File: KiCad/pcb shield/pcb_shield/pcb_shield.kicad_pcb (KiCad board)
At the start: 2 copper layers, 190 x 60 mm, 3 parts, among them J1 Raspberry Pi Zero, U1 BOB-09056

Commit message: start with pcb
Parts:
- added A3: Motor Controller Left, Module:Pololu_Breakout-16_15.2x20.3mm, F.Cu at (205.7, 87.6)
- added A4: Motor Controller Right, Module:Pololu_Breakout-16_15.2x20.3mm, F.Cu at (205.7, 110.5)
- added C1: C, Capacitor_THT:CP_Radial_D5.0mm_P2.50mm, F.Cu at (194.3, 81.3)
- added C2: C, Capacitor_THT:CP_Radial_D5.0mm_P2.50mm, F.Cu at (194.3, 104.1)
- added J1: , Connector_PinHeader_2.54mm:PinHeader_2x04_P2.54mm_Vertical, F.Cu at (86.4, 120.6)
- added J10: Motor Conn L, Connector_PinHeader_2.54mm:PinHeader_1x04_P2.54mm_Vertical, F.Cu at (236.2, 77.5)
- added J11: Motor Conn R, Connector_PinHeader_2.54mm:PinHeader_1x04_P2.54mm_Vertical, F.Cu at (236.2, 101.6)
- added J12: Endstop X, Connector_PinHeader_2.54mm:PinHeader_1x02_P2.54mm_Vertical, F.Cu at (172.7, 86.4)
- added J13: Endstop Y, Connector_PinHeader_2.54mm:PinHeader_1x02_P2.54mm_Vertical, F.Cu at (172.7, 78.7)
- added J2: , Connector_PinHeader_2.54mm:PinHeader_2x04_P2.54mm_Vertical, F.Cu at (74.9, 120.6)
- added J3: , Connector_PinHeader_2.54mm:PinHeader_2x04_P2.54mm_Vertical, F.Cu at (158.8, 120.6)
- added J4: , Connector_PinHeader_2.54mm:PinHeader_2x04_P2.54mm_Vertical, F.Cu at (147.3, 120.6)
- added J5: , Connector_PinHeader_2.54mm:PinHeader_2x04_P2.54mm_Vertical, F.Cu at (110.5, 120.6)
- added J6: , Connector_PinHeader_2.54mm:PinHeader_2x04_P2.54mm_Vertical, F.Cu at (99.1, 120.6)
- added J7: , Connector_PinHeader_2.54mm:PinHeader_2x04_P2.54mm_Vertical, F.Cu at (134.6, 120.6)
- added J8: , Connector_PinHeader_2.54mm:PinHeader_2x04_P2.54mm_Vertical, F.Cu at (123.2, 120.6)
- added J9: E_Magnet, Connector_PinHeader_2.54mm:PinHeader_1x02_P2.54mm_Vertical, F.Cu at (172.7, 96.5)
- added Q1: TIP120, Package_TO_SOT_THT:TO-220-3_Vertical, F.Cu at (172.7, 109.2)
- added U2: BOB-09056, BOB-09056:MODULE_BOB-09056, F.Cu at (148.6, 96.5)
- added U3: BOB-09056, BOB-09056:MODULE_BOB-09056, F.Cu at (100.3, 96.5)
- added U4: BOB-09056, BOB-09056:MODULE_BOB-09056, F.Cu at (124.5, 96.5)
- moved A1 49.5 mm to (120.7, 67.3)
- moved U1 2.33 mm to (76.2, 96.5)
- renumbered J1 to A1, A1 to A2
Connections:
- A1 pad 20: GND -> Net-(A1-Pad20)
- A1 pad 24: 14 TXD -> /14 TXD
- A1 pad 25: 18 RXD -> /18 RXD
- A1 pad 4: 4 -> Net-(A1-Pad4)
- A1 pad 6: 17 -> Net-(A1-Pad6)
- A1 pad 7: 27 -> Net-(A1-Pad7)
- A1 pad 8: 22 -> Net-(A1-Pad8)
- A2 pad 15: unconnected-(A1-Pad15) -> /14 TXD
- A2 pad 16: unconnected-(A1-Pad16) -> /18 RXD
- A2 pad 17: unconnected-(A1-Pad17) -> Net-(A2-Pad17)
- A2 pad 18: unconnected-(A1-Pad18) -> Net-(A2-Pad18)
- A2 pad 20: unconnected-(A1-Pad20) -> Net-(A3-Pad16)
- A2 pad 21: unconnected-(A1-Pad21) -> Net-(A2-Pad21)
- A2 pad 23: unconnected-(A1-Pad23) -> Net-(A2-Pad23)
- A2 pad 24: unconnected-(A1-Pad24) -> Net-(A2-Pad24)
- A2 pad 25: unconnected-(A1-Pad25) -> Net-(A2-Pad25)
- A2 pad 26: unconnected-(A1-Pad26) -> Net-(A2-Pad26)
- A2 pad 5: unconnected-(A1-Pad5) -> Net-(A4-Pad2)
- A2 pad 7: unconnected-(A1-Pad7) -> Net-(A2-Pad7)
- U1 pad JP1-1: unconnected-(U1-PadJP1-1) -> Net-(U1-PadJP1-1)
- U1 pad JP1-10: unconnected-(U1-PadJP1-10) -> Net-(U1-PadJP1-10)
- U1 pad JP1-11: unconnected-(U1-PadJP1-11) -> Net-(U1-PadJP1-11)
- U1 pad JP1-12: unconnected-(U1-PadJP1-12) -> Net-(U1-PadJP1-12)
- U1 pad JP1-13: unconnected-(U1-PadJP1-13) -> Net-(U1-PadJP1-13)
- U1 pad JP1-14: unconnected-(U1-PadJP1-14) -> Net-(U1-PadJP1-14)
- U1 pad JP1-15: unconnected-(U1-PadJP1-15) -> Net-(U1-PadJP1-15)
- U1 pad JP1-16: unconnected-(U1-PadJP1-16) -> Net-(U1-PadJP1-16)
- U1 pad JP1-2: unconnected-(U1-PadJP1-2) -> Net-(U1-PadJP1-2)
- U1 pad JP1-3: unconnected-(U1-PadJP1-3) -> Net-(U1-PadJP1-3)
- U1 pad JP1-4: unconnected-(U1-PadJP1-4) -> Net-(U1-PadJP1-4)
- U1 pad JP1-5: unconnected-(U1-PadJP1-5) -> Net-(U1-PadJP1-5)
- U1 pad JP1-6: unconnected-(U1-PadJP1-6) -> Net-(U1-PadJP1-6)
- U1 pad JP1-7: unconnected-(U1-PadJP1-7) -> Net-(U1-PadJP1-7)
- U1 pad JP1-8: unconnected-(U1-PadJP1-8) -> Net-(U1-PadJP1-8)
- U1 pad JP1-9: unconnected-(U1-PadJP1-9) -> Net-(U1-PadJP1-9)
- U1 pad JP3-1: unconnected-(U1-PadJP3-1) -> Net-(A1-Pad20)
- U1 pad JP3-2: unconnected-(U1-PadJP3-2) -> 5V
- U1 pad JP3-3: unconnected-(U1-PadJP3-3) -> Net-(A1-Pad4)
- U1 pad JP3-4: unconnected-(U1-PadJP3-4) -> Net-(U1-PadJP3-4)
- U1 pad JP3-5: unconnected-(U1-PadJP3-5) -> Net-(U1-PadJP3-5)
- U1 pad JP3-6: unconnected-(U1-PadJP3-6) -> Net-(U1-PadJP3-6)
- U1 pad JP3-7: unconnected-(U1-PadJP3-7) -> Net-(U1-PadJP3-7)
- U1 pad JP3-8: unconnected-(U1-PadJP3-8) -> Net-(U1-PadJP3-8)
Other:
- board size 190 x 60 mm -> 190 x 65 mm

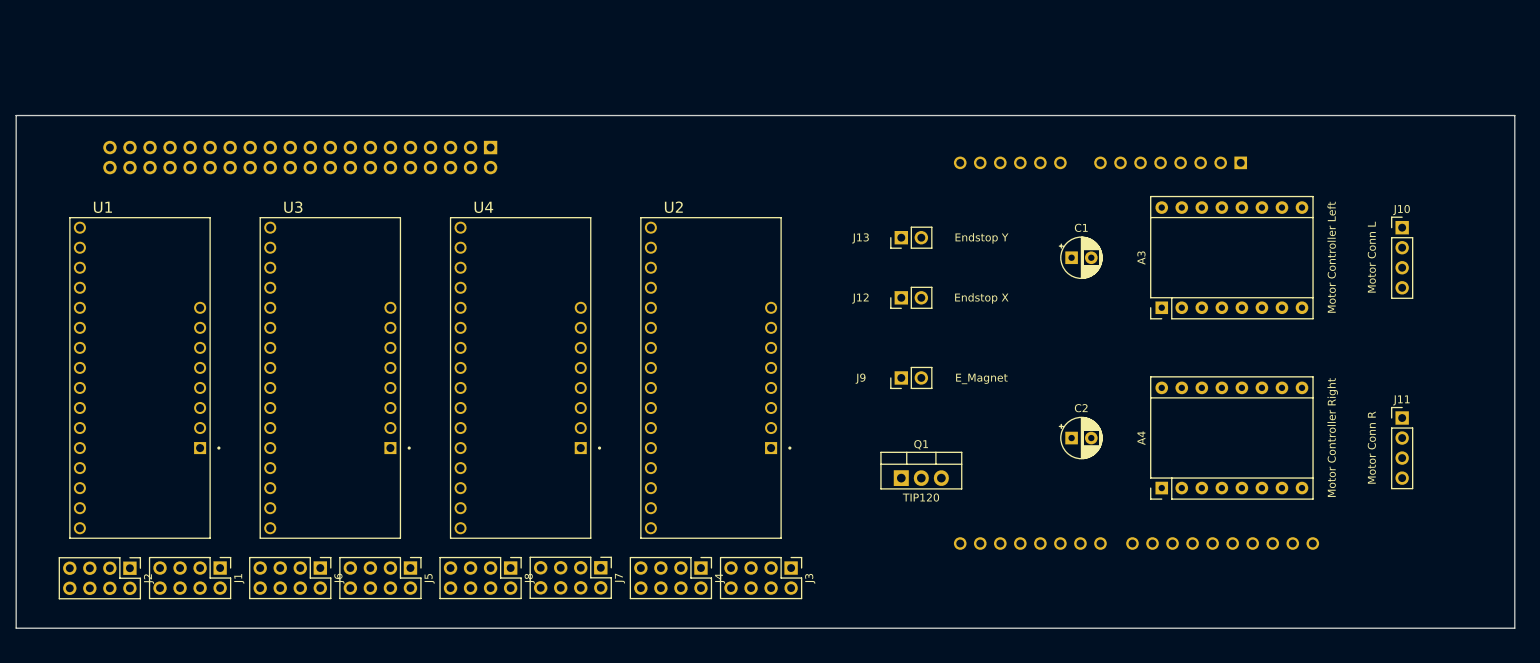
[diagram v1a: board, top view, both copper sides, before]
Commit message: adding multiplexers
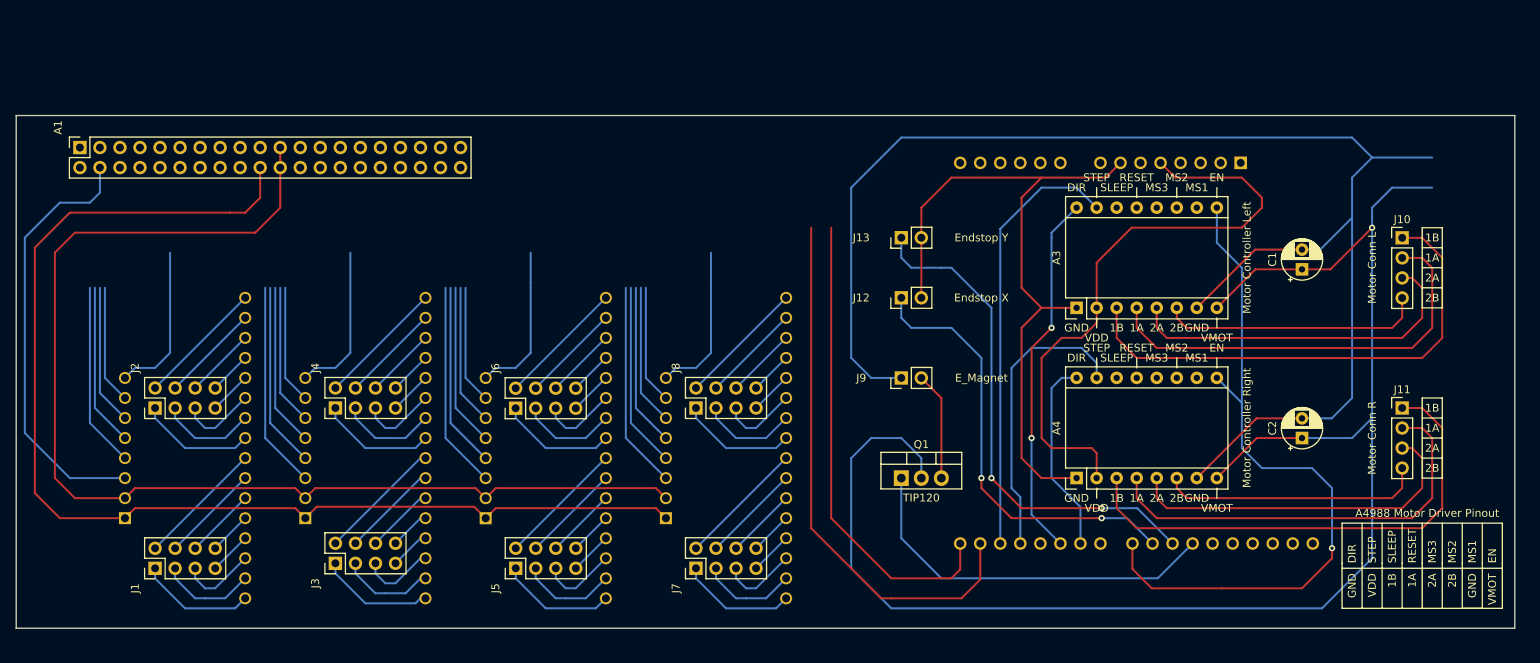
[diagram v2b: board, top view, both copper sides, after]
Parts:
- A1: moved to F.Cu
- U1, U2, U3, U4: moved to B.Cu
- moved J3 57.8 mm to (101.0, 120.0), turned to 90 degrees
- moved A1 52.1 mm to (68.6, 67.3)
- moved J4 50.6 mm to (101.0, 100.3), turned to 90 degrees
- moved U2 44.7 mm to (104.8, 105.4), turned to 180 degrees
- moved J6 32.0 mm to (123.8, 100.4), turned to 90 degrees
- moved J8 31.0 mm to (146.7, 100.3), turned to 90 degrees
- moved C1 29.2 mm to (223.5, 82.8), turned to 90 degrees
- moved C2 29.2 mm to (223.5, 104.1), turned to 90 degrees
- moved U3 28.7 mm to (127.6, 105.4), turned to 180 degrees
- moved U4 27.5 mm to (150.5, 105.4), turned to 180 degrees
- moved J2 20.6 mm to (78.1, 100.3), turned to 90 degrees
- moved J5 13.3 mm to (123.8, 120.7), turned to 90 degrees
- moved J7 12.1 mm to (146.7, 120.7), turned to 90 degrees
- moved A4 10.9 mm to (194.9, 109.2)
- moved A3 10.8 mm to (194.9, 87.6)
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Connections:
- J1 pad 2: Net-(U1-PadJP1-3) -> Net-(U1-PadJP1-8)
- J1 pad 3: Net-(U1-PadJP1-5) -> Net-(U1-PadJP1-2)
- J1 pad 5: Net-(U1-PadJP1-8) -> Net-(U1-PadJP1-3)
- J1 pad 8: Net-(U1-PadJP1-2) -> Net-(U1-PadJP1-5)
- J2 pad 2: Net-(U1-PadJP1-11) -> Net-(U1-PadJP1-16)
- J2 pad 3: Net-(U1-PadJP1-13) -> Net-(U1-PadJP1-10)
- J2 pad 5: Net-(U1-PadJP1-16) -> Net-(U1-PadJP1-11)
- J2 pad 8: Net-(U1-PadJP1-10) -> Net-(U1-PadJP1-13)
- J3 pad 2: Net-(J3-Pad2) -> Net-(U2-PadJP1-8)
- J3 pad 3: Net-(J3-Pad3) -> Net-(U2-PadJP1-2)
- J3 pad 5: Net-(J3-Pad5) -> Net-(U2-PadJP1-3)
- J3 pad 8: Net-(J3-Pad8) -> Net-(U2-PadJP1-5)
- J4 pad 2: Net-(J4-Pad2) -> Net-(U2-PadJP1-16)
- J4 pad 3: Net-(J4-Pad3) -> Net-(U2-PadJP1-10)
- J4 pad 5: Net-(J4-Pad5) -> Net-(U2-PadJP1-11)
- J4 pad 8: Net-(J4-Pad8) -> Net-(U2-PadJP1-13)
- J5 pad 2: Net-(J5-Pad2) -> Net-(U3-PadJP1-8)
- J5 pad 3: Net-(J5-Pad3) -> Net-(U3-PadJP1-2)
- J5 pad 5: Net-(J5-Pad5) -> Net-(U3-PadJP1-3)
- J5 pad 8: Net-(J5-Pad8) -> Net-(U3-PadJP1-5)
- J6 pad 2: Net-(J6-Pad2) -> Net-(U3-PadJP1-16)
- J6 pad 3: Net-(J6-Pad3) -> Net-(U3-PadJP1-10)
- J6 pad 5: Net-(J6-Pad5) -> Net-(U3-PadJP1-11)
- J6 pad 8: Net-(J6-Pad8) -> Net-(U3-PadJP1-13)
- J7 pad 2: Net-(J7-Pad2) -> Net-(U4-PadJP1-8)
- J7 pad 3: Net-(J7-Pad3) -> Net-(U4-PadJP1-2)
- J7 pad 5: Net-(J7-Pad5) -> Net-(U4-PadJP1-3)
- J7 pad 8: Net-(J7-Pad8) -> Net-(U4-PadJP1-5)
- J8 pad 2: Net-(J8-Pad2) -> Net-(U4-PadJP1-16)
- J8 pad 3: Net-(J8-Pad3) -> Net-(U4-PadJP1-10)
- J8 pad 5: Net-(J8-Pad5) -> Net-(U4-PadJP1-11)
- J8 pad 8: Net-(J8-Pad8) -> Net-(U4-PadJP1-13)
- U2 pad JP1-10: Net-(J4-Pad8) -> Net-(U2-PadJP1-10)
- U2 pad JP1-11: Net-(J4-Pad2) -> Net-(U2-PadJP1-11)
- U2 pad JP1-13: Net-(J4-Pad3) -> Net-(U2-PadJP1-13)
- U2 pad JP1-16: Net-(J4-Pad5) -> Net-(U2-PadJP1-16)
- U2 pad JP1-2: Net-(J3-Pad8) -> Net-(U2-PadJP1-2)
- U2 pad JP1-3: Net-(J3-Pad2) -> Net-(U2-PadJP1-3)
- U2 pad JP1-5: Net-(J3-Pad3) -> Net-(U2-PadJP1-5)
- U2 pad JP1-8: Net-(J3-Pad5) -> Net-(U2-PadJP1-8)
- U3 pad JP1-10: Net-(J6-Pad8) -> Net-(U3-PadJP1-10)
- U3 pad JP1-11: Net-(J6-Pad2) -> Net-(U3-PadJP1-11)
- U3 pad JP1-13: Net-(J6-Pad3) -> Net-(U3-PadJP1-13)
- U3 pad JP1-16: Net-(J6-Pad5) -> Net-(U3-PadJP1-16)
- U3 pad JP1-2: Net-(J5-Pad8) -> Net-(U3-PadJP1-2)
- U3 pad JP1-3: Net-(J5-Pad2) -> Net-(U3-PadJP1-3)
- U3 pad JP1-5: Net-(J5-Pad3) -> Net-(U3-PadJP1-5)
- U3 pad JP1-8: Net-(J5-Pad5) -> Net-(U3-PadJP1-8)
- U4 pad JP1-10: Net-(J8-Pad8) -> Net-(U4-PadJP1-10)
- U4 pad JP1-11: Net-(J8-Pad2) -> Net-(U4-PadJP1-11)
- U4 pad JP1-13: Net-(J8-Pad3) -> Net-(U4-PadJP1-13)
- U4 pad JP1-16: Net-(J8-Pad5) -> Net-(U4-PadJP1-16)
- U4 pad JP1-2: Net-(J7-Pad8) -> Net-(U4-PadJP1-2)
- U4 pad JP1-3: Net-(J7-Pad2) -> Net-(U4-PadJP1-3)
- U4 pad JP1-5: Net-(J7-Pad3) -> Net-(U4-PadJP1-5)
- U4 pad JP1-8: Net-(J7-Pad5) -> Net-(U4-PadJP1-8)
- U4 pad JP3-4: unconnected-(U4-PadJP3-4) -> Net-(U1-PadJP3-4)
- U4 pad JP3-5: unconnected-(U4-PadJP3-5) -> Net-(U1-PadJP3-5)
- U4 pad JP3-6: unconnected-(U4-PadJP3-6) -> Net-(U1-PadJP3-6)
- U4 pad JP3-7: unconnected-(U4-PadJP3-7) -> Net-(U1-PadJP3-7)
- U4 pad JP3-8: unconnected-(U4-PadJP3-8) -> Net-(U1-PadJP3-8)
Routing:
- net Net-(A4-Pad8): track 0.00 -> 198.1 mm, vias 0 -> 1
- net Net-(A4-Pad7): track 0.00 -> 186.2 mm
- net Net-(A1-Pad20): track 0.00 -> 150.8 mm
- net 5V: track 0.00 -> 148.8 mm
- net Net-(U1-PadJP3-4): track 0.00 -> 93.7 mm
- net Net-(A2-Pad23): track 0.00 -> 90.5 mm, vias 0 -> 1
- net Net-(A2-Pad7): track 0.00 -> 90.2 mm
- net Net-(U1-PadJP3-5): track 0.00 -> 82.5 mm
- net Net-(U1-PadJP3-8): track 0.00 -> 78.9 mm
- net Net-(A4-Pad2): track 0.00 -> 77.3 mm
- net Net-(U1-PadJP3-6): track 0.00 -> 71.3 mm
- net /18 RXD: track 0.00 -> 68.8 mm
- net Net-(A2-Pad25): track 0.00 -> 64.6 mm, vias 0 -> 2
- net Net-(A4-Pad3): track 0.00 -> 63.5 mm
- net Net-(A3-Pad3): track 0.00 -> 63.5 mm
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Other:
- board text added: "1A"
- board text added: "1B"
- board text added: "2A"
- board text added: "2B"
- board text added: "A4988 Motor Driver Pinout"
- board text added: "DIR"
- board text added: "EN"
- board text added: "GND"
- board text added: "J1"
- board text added: "MS1"
- board text added: "MS2"
- board text added: "MS3"
- board text added: "RESET"
- board text added: "SLEEP"
- board text added: "STEP"
- board text added: "VDD"
- board text added: "VMOT"

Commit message: almost finished pcb
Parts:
- A1: moved to B.Cu
- moved A1 50.8 mm to (119.4, 68.6)
- moved A3 1.27 mm to (194.9, 88.9)
- moved A4 1.27 mm to (194.9, 110.5)
- moved J13 1.27 mm to (172.7, 80.0)
- moved J2 1.27 mm to (78.1, 101.6)
- moved J3 1.27 mm to (101.0, 121.3)
- moved J9 1.27 mm to (172.7, 97.8)
- moved U1 1.27 mm to (81.9, 106.7)
- moved U2 1.27 mm to (104.8, 106.7)
- moved U4 1.27 mm to (150.5, 106.7)
- moved A2 1.27 mm to (215.8, 70.5)
- moved C1 1.27 mm to (223.5, 84.0)
- moved C2 1.27 mm to (223.5, 105.4)
- moved J1 1.27 mm to (78.1, 121.9)
- moved J10 1.27 mm to (236.2, 80.0)
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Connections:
- A1 pad 15: 5 -> Net-(A1-Pad15)
- A1 pad 16: 6 -> Net-(A1-Pad16)
- A1 pad 17: 13 -> Net-(A1-Pad17)
- A1 pad 18: 19 -> Net-(A1-Pad18)
- A1 pad 19: 26 -> Net-(A1-Pad19)
- U1 pad JP3-3: Net-(A1-Pad4) -> Net-(A1-Pad8)
- U1 pad JP3-4: Net-(U1-PadJP3-4) -> Net-(A1-Pad19)
- U1 pad JP3-5: Net-(U1-PadJP3-5) -> Net-(A1-Pad18)
- U1 pad JP3-6: Net-(U1-PadJP3-6) -> Net-(A1-Pad17)
- U1 pad JP3-7: Net-(U1-PadJP3-7) -> Net-(A1-Pad16)
- U1 pad JP3-8: Net-(U1-PadJP3-8) -> Net-(A1-Pad15)
- U2 pad JP3-4: Net-(U1-PadJP3-4) -> Net-(A1-Pad19)
- U2 pad JP3-5: Net-(U1-PadJP3-5) -> Net-(A1-Pad18)
- U2 pad JP3-6: Net-(U1-PadJP3-6) -> Net-(A1-Pad17)
- U2 pad JP3-7: Net-(U1-PadJP3-7) -> Net-(A1-Pad16)
- U2 pad JP3-8: Net-(U1-PadJP3-8) -> Net-(A1-Pad15)
- U3 pad JP3-4: Net-(U1-PadJP3-4) -> Net-(A1-Pad19)
- U3 pad JP3-5: Net-(U1-PadJP3-5) -> Net-(A1-Pad18)
- U3 pad JP3-6: Net-(U1-PadJP3-6) -> Net-(A1-Pad17)
- U3 pad JP3-7: Net-(U1-PadJP3-7) -> Net-(A1-Pad16)
- U3 pad JP3-8: Net-(U1-PadJP3-8) -> Net-(A1-Pad15)
- U4 pad JP3-3: Net-(A1-Pad8) -> Net-(A1-Pad4)
- U4 pad JP3-4: Net-(U1-PadJP3-4) -> Net-(A1-Pad19)
- U4 pad JP3-5: Net-(U1-PadJP3-5) -> Net-(A1-Pad18)
- U4 pad JP3-6: Net-(U1-PadJP3-6) -> Net-(A1-Pad17)
- U4 pad JP3-7: Net-(U1-PadJP3-7) -> Net-(A1-Pad16)
- U4 pad JP3-8: Net-(U1-PadJP3-8) -> Net-(A1-Pad15)
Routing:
- net Net-(A1-Pad16): track 0.00 -> 173.4 mm
- net Net-(A1-Pad15): track 0.00 -> 134.7 mm
- net Net-(A1-Pad19): track 0.00 -> 114.2 mm
- net Net-(A1-Pad18): track 0.00 -> 111.2 mm
- net Net-(A1-Pad17): track 0.00 -> 108.3 mm
- net Net-(U1-PadJP3-4): track 93.7 -> 0.00 mm
- net Net-(U1-PadJP3-5): track 82.5 -> 0.00 mm
- net Net-(U1-PadJP3-8): track 78.9 -> 0.00 mm
- net Net-(U1-PadJP3-6): track 71.3 -> 0.00 mm
- net /14 TXD: track 60.1 -> 124.6 mm, vias 0 -> 1
- net /18 RXD: track 68.8 -> 131.8 mm
- net Net-(U1-PadJP3-7): track 60.1 -> 0.00 mm
- net Net-(A1-Pad8): track 26.2 -> 75.3 mm
- net Net-(A1-Pad6): track 26.2 -> 44.9 mm
- net Net-(U2-PadJP3-3): track 26.2 -> 44.4 mm
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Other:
- board text added: "1"
- board text added: "10"
- board text added: "11"
- board text added: "12"
- board text added: "13"
- board text added: "14"
- board text added: "15"
- board text added: "16"
- board text added: "2"
- board text added: "3"
- board text added: "3V3"
- board text added: "4"
- board text added: "5"
- board text added: "5V"
- board text added: "6"
- board text added: "7"
- board text added: "8"
- board text added: "9"
- board text added: "C0"
- board text added: "C1"
- board text added: "C10"
- board text added: "C11"
- board text added: "C12"
- board text added: "C13"
- board text added: "C14"
- board text added: "C15"
- board text added: "C2"
- board text added: "C3"
- board text added: "C4"
- board text added: "C5"
- board text added: "C6"
- board text added: "C7"
- board text added: "C8"
- board text added: "C9"
- board text added: "COM"
- board text added: "S0"
- board text added: "S1"
- board text added: "S2"
- board text added: "S3"
- board text removed: "J1"
